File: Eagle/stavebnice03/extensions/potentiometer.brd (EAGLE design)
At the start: 6 parts

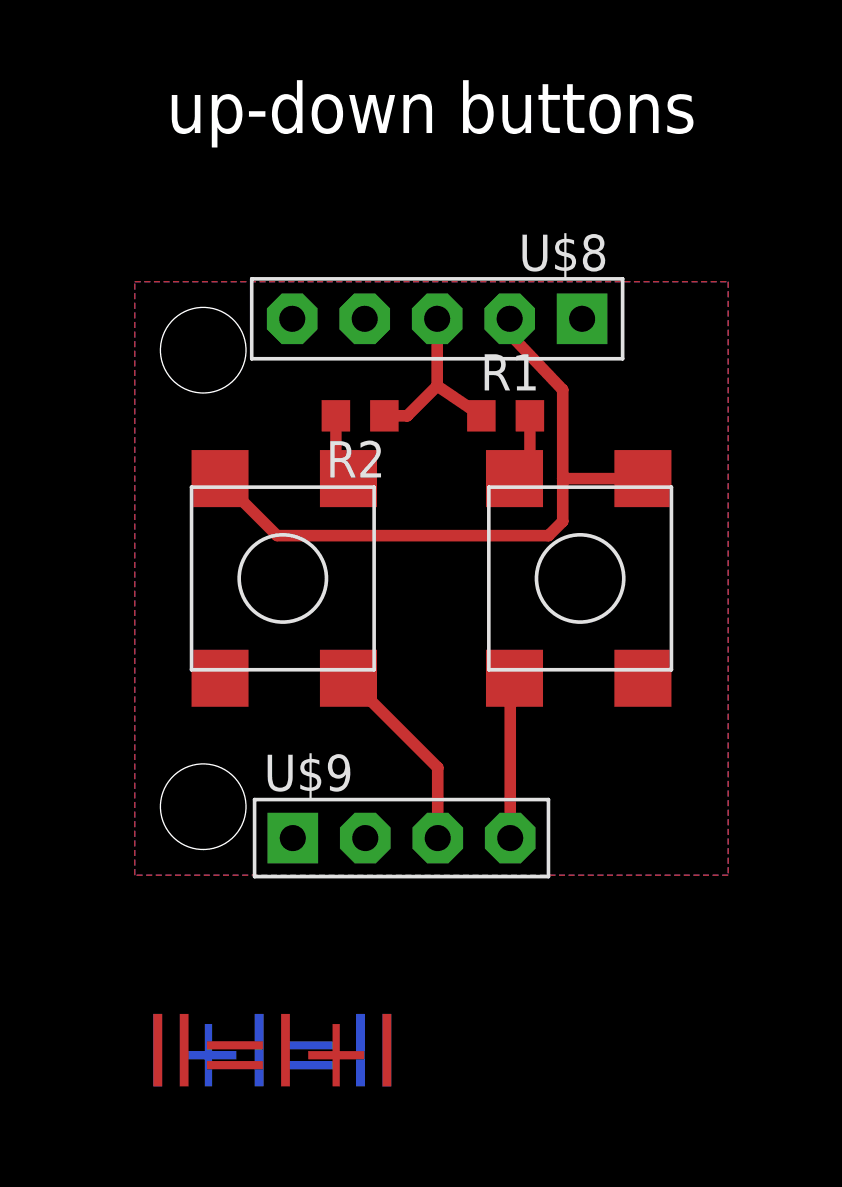
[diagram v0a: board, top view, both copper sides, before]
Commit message: eagle adjustment for the Jíťa version
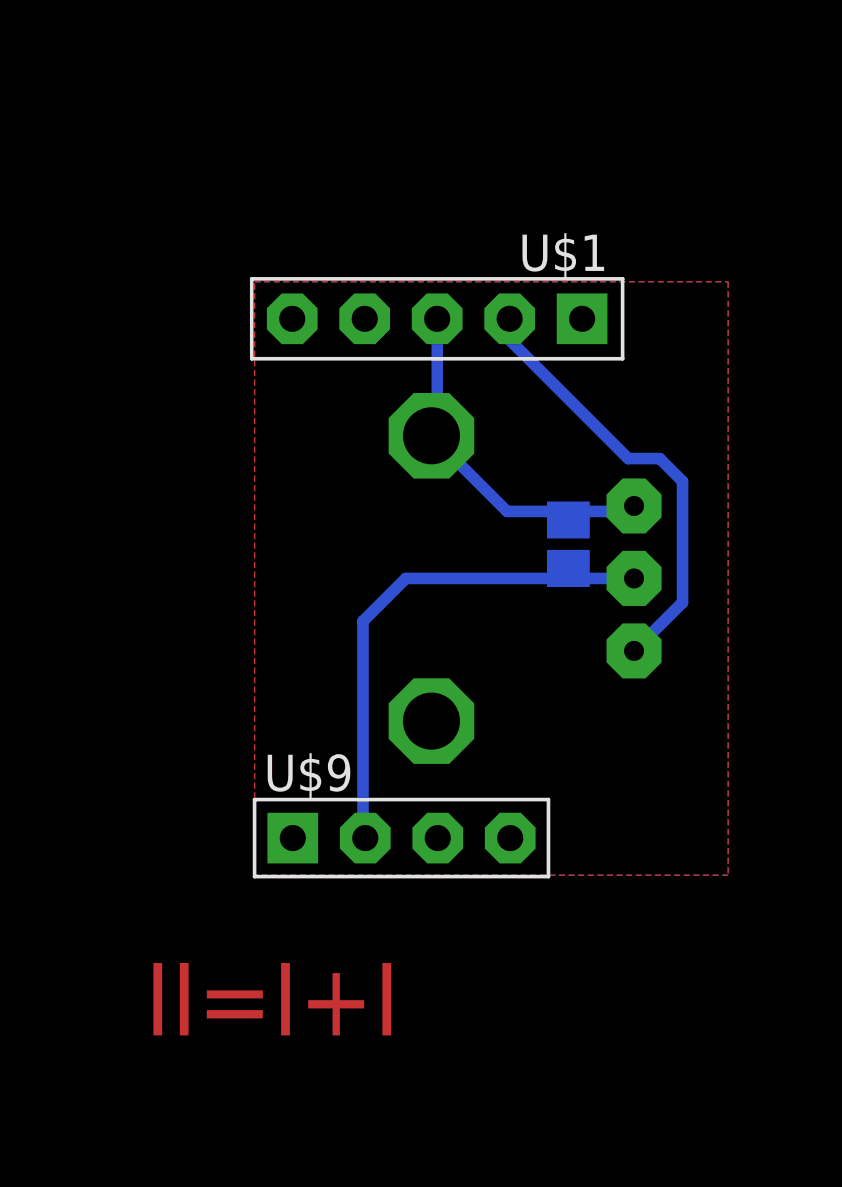
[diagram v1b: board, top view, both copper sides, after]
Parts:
- removed R1, R2: 100k, resistor:R0603
- removed U$8: JUMPER5M, !stavebnice03:JUMPER5M
- added C1: 100 nF, resistor:C0805
- U$1: value BUTTON_6.3X6.3 -> JUMPER5M; device !stavebnice03:BUTTON_6.2X6.2 -> !stavebnice03:JUMPER5M
- U$2: value BUTTON_6.3X6.3 -> POTENTIOMETER-RK09; device !stavebnice03:BUTTON_6.2X6.2 -> !stavebnice03:POTENTIOMETER-RK09
- moved U$1 10.4 mm to (10.7, 19.6)
- moved U$2 5.20 mm to (10.5, 10.5), turned to 270 degrees
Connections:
- removed net N$4: R1.2, U$1.P$2, U$1.P$4, U$9.4
- net GND: now also C1.2, U$1.3, U$2.1, U$2.GND1, U$2.GND2; no longer R1.1, R2.1, U$8.3
- net N$1: now also C1.1, U$2.2, U$9.2; no longer R2.2, U$2.P$2, U$2.P$4, U$9.3
- net N$2: now also U$1.2, U$2.3; no longer U$1.P$1, U$1.P$3, U$2.P$1, U$2.P$3, U$8.2
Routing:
- net N$4: track 8.85 -> 0.00 mm
- net N$2: track 24.3 -> 15.5 mm
- net N$1: track 9.49 -> 18.0 mm
- net GND: track 6.51 -> 12.9 mm
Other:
- board text added: "potentiometer"
- board text removed: "up-down buttons"
